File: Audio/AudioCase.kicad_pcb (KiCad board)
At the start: 2 copper layers, 677.1 x 246.6 mm, 224 parts, among them J10 AMP_AUX_IN, J11 AMP_AUX_OUT, J12 AMP1_PWR, J13 ROTARY_SW, J14 AMP_PWR_IN, J15 PD_IN, J16 AUDIO_IN, J17 OLED_PIN, J18 AMP1_LR, J19 AMP2_PWR, J20 AMP2_LR, J21 AMP3_PWR, J22 AMP4_PWR, J23 AMP5_PWR, J24 AMP3_LR, J25 AMP4_LR, J26 AMP5_LR, J29 Conn_01x06_Pin, J30 Conn_01x06_Pin, J4 PWR_IN, J5 PWR_OUT, J6 AUX_IN, J7 V_IN, J701 AUDIO, J702 V_IN, J703 15_V_IN, J8 AUX_OUT, J9 AMP_PWR, K1 AZ850P2-x, K10 AZ850P2-x, K2 AZ850P2-x, K3 AZ850P2-x, K4 AZ850P2-x, K5 AZ850P2-x, K6 AZ850P2-x, K7 AZ850P2-x, K8 AZ850P2-x, K9 AZ850P2-x, U1 MCW03, U2 NJM4558, U3 NJM4558, U4 NJM4558, U5 BP5293-50, U6 ULN2803A, U7 ULN2803A, U701 OPA1656, U702 OPA1656, U703 OPA1656, U704 BP5293-50, U705 MBC2596-01, U706 LT1763-3.3, U707 LT1763-5, U708 XC8107AC20MR-G, U709 TPS3808G33DBVR, U710 TPS3808G50DBVR, U8 ULN2803A, Y701 ASFL1-12.288MHZ-EC-T

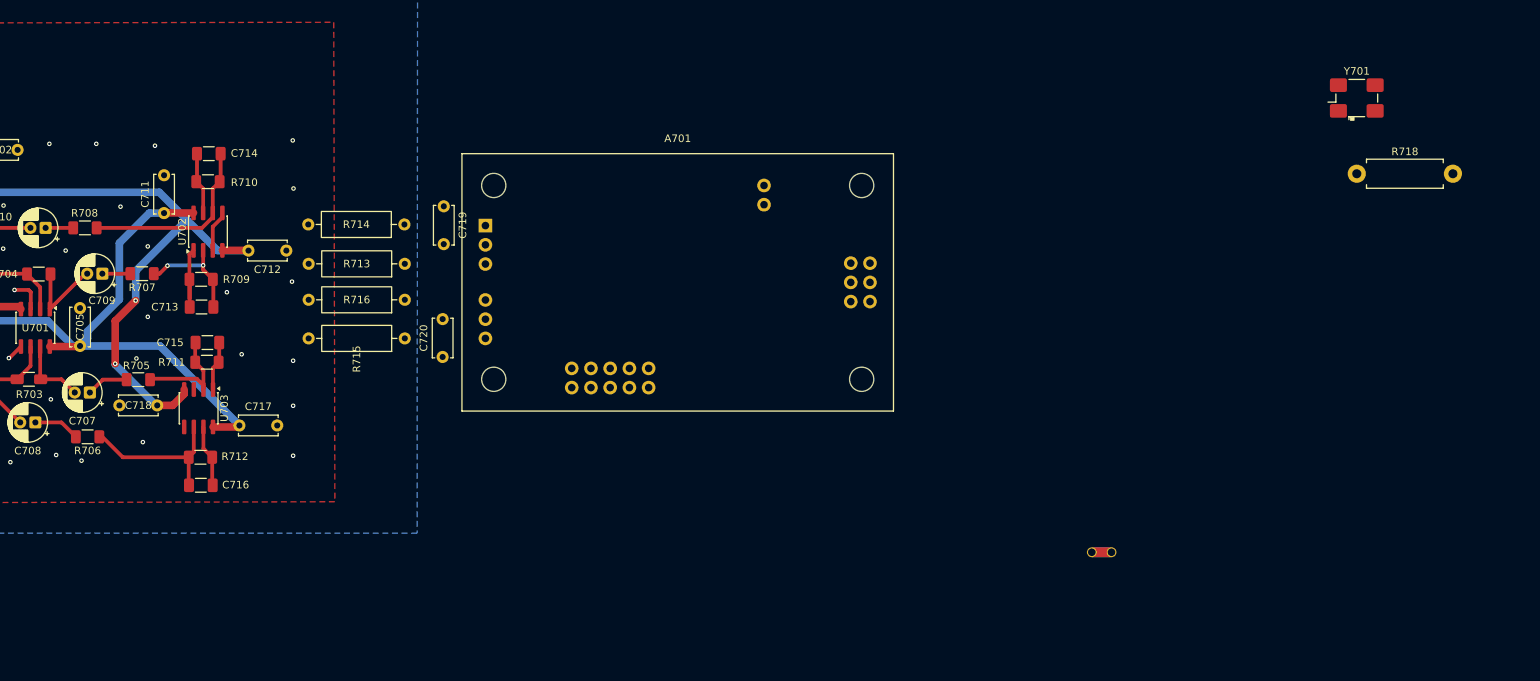
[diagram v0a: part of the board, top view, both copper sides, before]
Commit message: wip: MeasurementADCのOPA周辺配置とVCOM/VIN配線を途中保存する。
A701側へC719/C720・R713–716を寄せ、VCOML/RとVIN±の幹線を引き始めた状態。

Co-authored-by: Cursor <cursoragent@cursor.com>
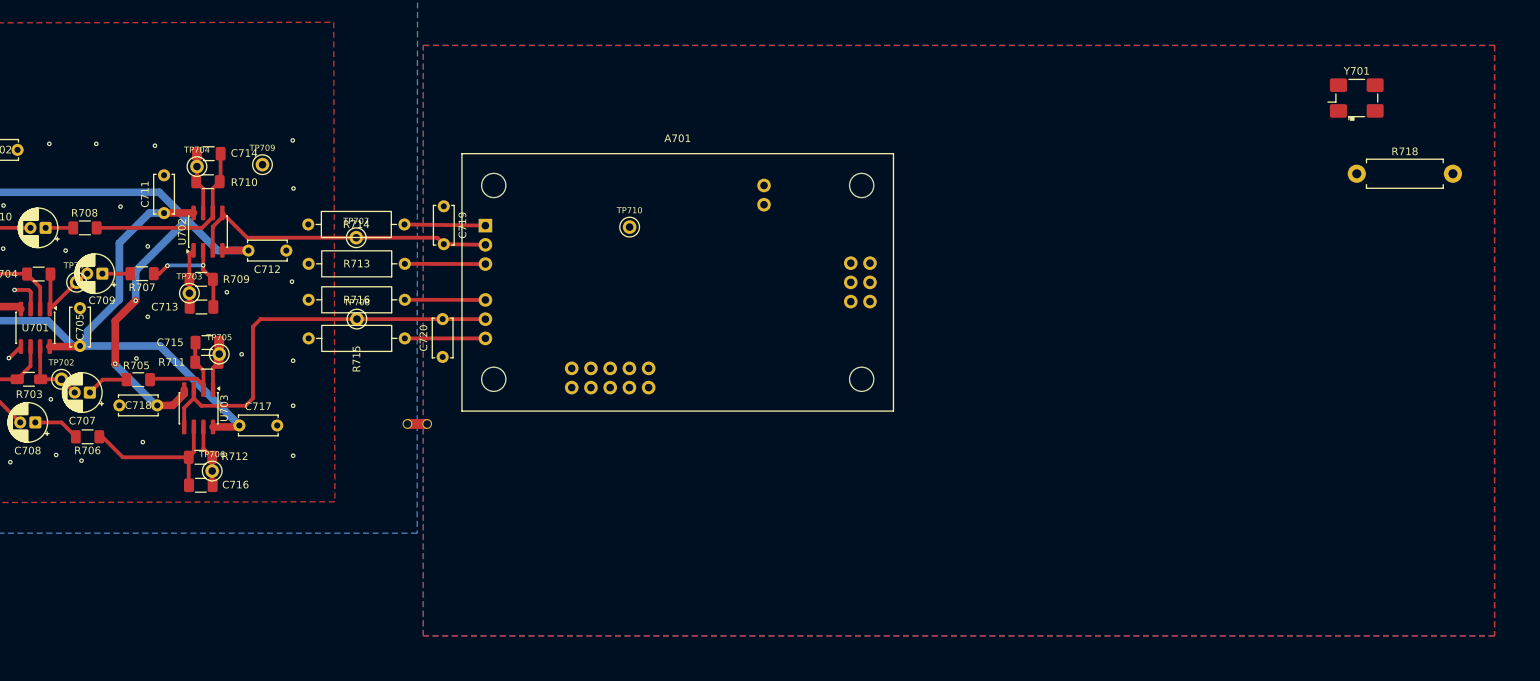
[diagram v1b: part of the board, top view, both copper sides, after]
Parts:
- added TP701: TestPoint, TestPoint:TestPoint_THTPad_1.0x1.0mm_Drill0.7mm, F.Cu at (374.7, 131.3)
- added TP702: TestPoint, TestPoint:TestPoint_THTPad_1.0x1.0mm_Drill0.7mm, F.Cu at (372.7, 144.1)
- added TP703: TestPoint, TestPoint:TestPoint_THTPad_1.0x1.0mm_Drill0.7mm, F.Cu at (389.6, 132.7)
- added TP704: TestPoint, TestPoint:TestPoint_THTPad_1.0x1.0mm_Drill0.7mm, F.Cu at (390.6, 116.0)
- added TP705: TestPoint, TestPoint:TestPoint_THTPad_1.0x1.0mm_Drill0.7mm, F.Cu at (393.5, 140.8)
- added TP706: TestPoint, TestPoint:TestPoint_THTPad_1.0x1.0mm_Drill0.7mm, F.Cu at (392.6, 156.2)
- added TP707: TestPoint, TestPoint:TestPoint_THTPad_1.0x1.0mm_Drill0.7mm, F.Cu at (411.6, 125.4)
- added TP708: TestPoint, TestPoint:TestPoint_THTPad_1.0x1.0mm_Drill0.7mm, F.Cu at (411.7, 136.2)
- added TP709: TestPoint, TestPoint:TestPoint_THTPad_1.0x1.0mm_Drill0.7mm, F.Cu at (399.2, 115.8)
- added TP710: TestPoint, TestPoint:TestPoint_THTPad_1.0x1.0mm_Drill0.7mm, F.Cu at (447.8, 124.0)
- moved NT701 89.4 mm to (421.0, 150.0), turned to 180 degrees
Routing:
- net /MeasurementADC/VCOMR: track 0.00 -> 54.7 mm
- net /MeasurementADC/VCOML: track 5.48 -> 41.9 mm
- net /MeasurementADC/VINL+: track 0.00 -> 10.7 mm
- net /MeasurementADC/VINL-: track 0.00 -> 10.7 mm
- net /MeasurementADC/VINR+: track 0.00 -> 10.7 mm
- net /MeasurementADC/VINR-: track 0.00 -> 10.6 mm
- added copper zone on B.Cu, net /MeasurementADC/ADC_GND
- added copper zone on F.Cu, net /MeasurementADC/ADC_GND

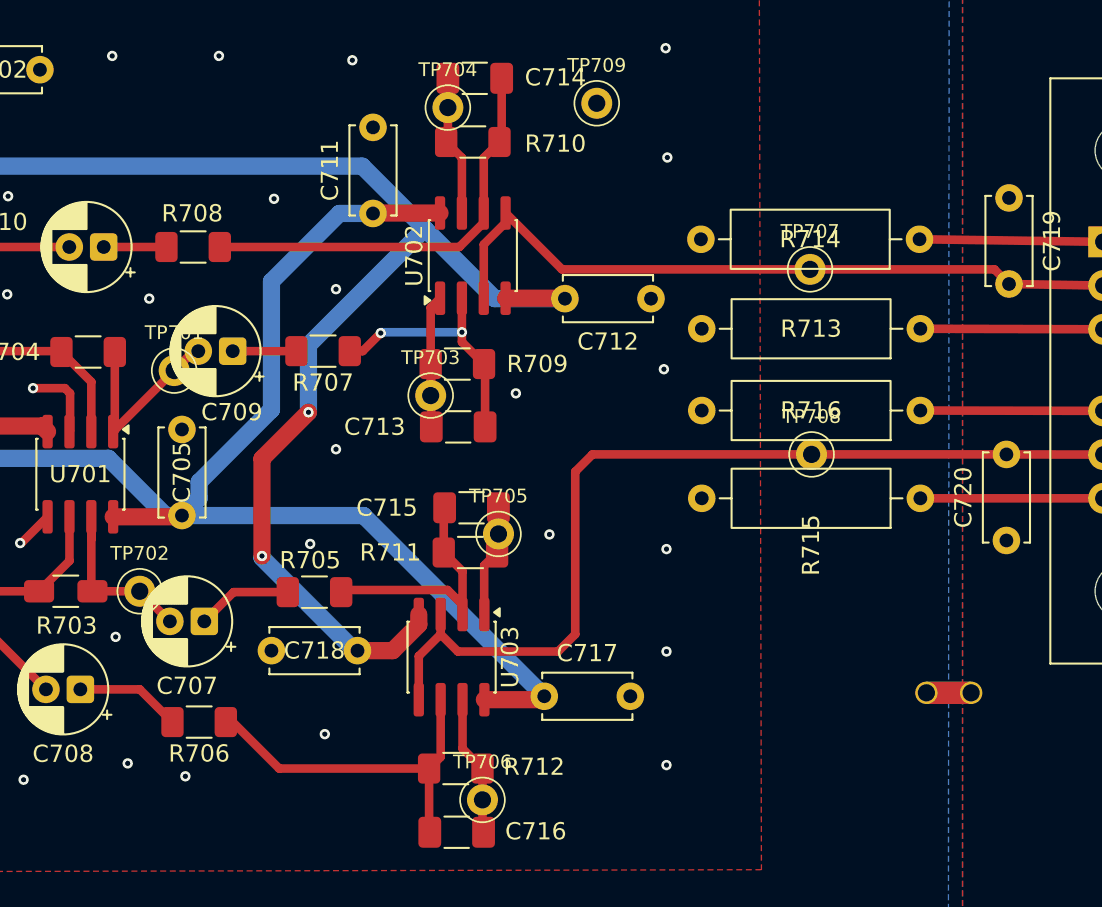
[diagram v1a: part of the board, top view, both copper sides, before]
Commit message: wip: VCOM/VIN導通とADC_GNDベタを進め、STATUSとgitignoreを更新する。
OPA〜A701のVCOM/VINをパッドまで閉じ、NT701境界とADC_GNDベタ・TPを追加。

Co-authored-by: Cursor <cursoragent@cursor.com>
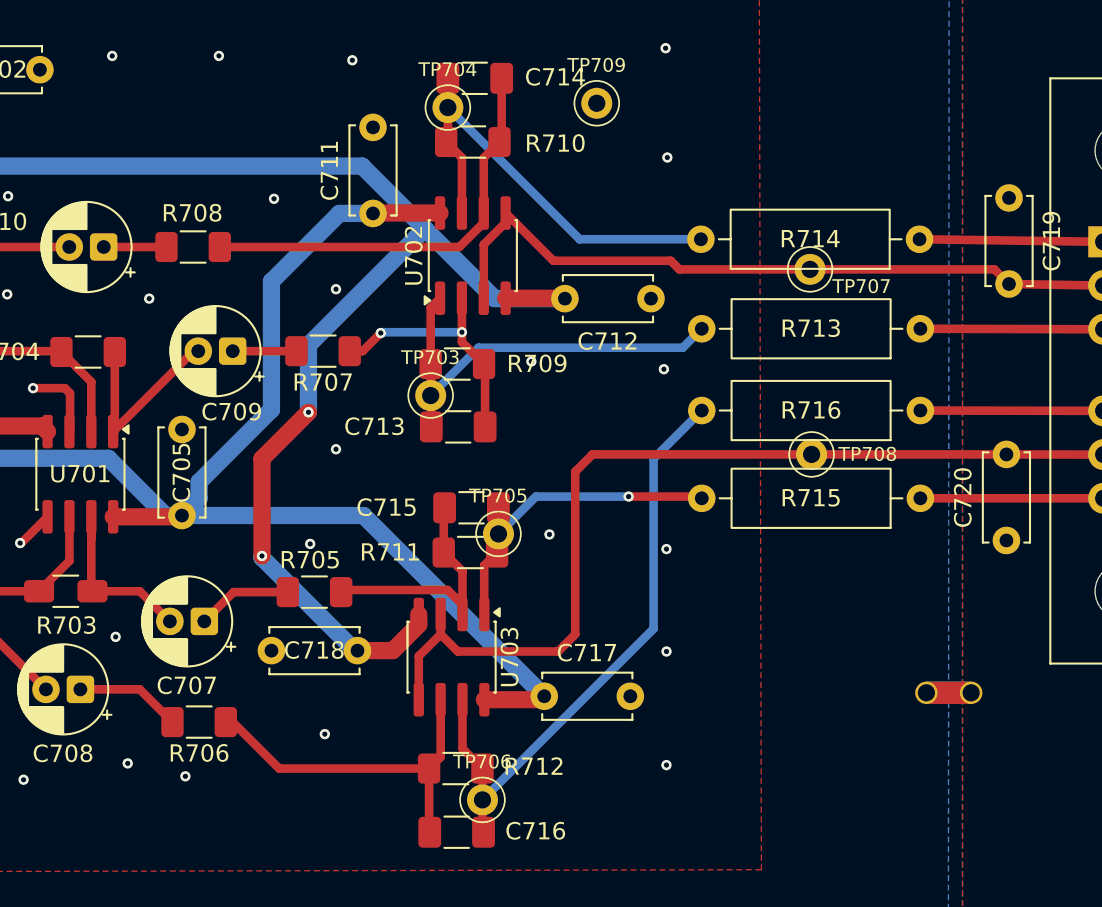
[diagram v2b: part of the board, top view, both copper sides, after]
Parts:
- removed TP701, TP702: TestPoint, TestPoint:TestPoint_THTPad_1.0x1.0mm_Drill0.7mm
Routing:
- net Net-(U703B-OUTB): track 8.21 -> 36.1 mm
- net Net-(U702B-OUTB): track 8.25 -> 26.1 mm
- net Net-(U702A-OUTA): track 10.3 -> 27.6 mm
- net Net-(U703A-OUTA): track 6.55 -> 19.3 mm, vias 0 -> 1

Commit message: ムラタRDEのフットプリントを実寸に合わせ、STATUSを現状に更新する。
Disc φ5汎用FPが過大で干渉誤認の原因だったため、発注品RDER71Hに合わせたFPへ20箇所を差し替える。

Co-authored-by: Cursor <cursoragent@cursor.com>
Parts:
- C701, C702, C705, C706, C711, C712, C717, C718, C719, C720, C722, C724, C725, C728, C730, C731, C735, C736, C737, C738: footprint Capacitor_THT:C_Disc_D5.0mm_W2.5mm_P5.00mm -> Library:C_Murata_RDE_L4.0mm_W3.5mm_T2.5mm_P5.00mm
